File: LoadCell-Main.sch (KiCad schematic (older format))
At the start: 13 parts, among them J1 0.100_1X4, J2 22-27-2031, U1 LMV358

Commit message: Generated revA output files
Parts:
- gave numbers to parts that had none: 1
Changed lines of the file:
@@
 	5650 3650 5700 3650
 Wire Wire Line
-	5700 3950 5700 4000
-Wire Wire Line
-	5700 4000 5700 4050
+	5700 3950 5700 4050
 Wire Wire Line
 	5050 3750 5000 3750
@@
 Connection ~ 6250 4450
 Wire Wire Line
-	6900 3950 6900 4000
-Wire Wire Line
-	6900 4000 6900 4050
+	6900 3950 6900 4050
 Wire Wire Line
 	6900 4450 6900 4350
@@
 $EndComp
 Wire Wire Line
-	6650 3650 6700 3650
-Wire Wire Line
-	6700 3650 6900 3650
-Wire Wire Line
-	6900 3650 7150 3650
-Wire Wire Line
-	7150 3650 7450 3650
+	6650 3650 7450 3650
 Wire Wire Line
 	7750 4450 7750 4200
@@
 Connection ~ 7750 3250
 Wire Wire Line
-	8000 3350 8000 4450
-Wire Wire Line
-	8000 4450 8000 4600
+	8000 3350 8000 4600
 Wire Wire Line
 	8000 3350 8100 3350
@@
 	4700 3350 4700 4450
 Wire Wire Line
-	4700 4450 5250 4450
-Wire Wire Line
-	5250 4450 6250 4450
-Wire Wire Line
-	6250 4450 6900 4450
-Wire Wire Line
-	6900 4450 7150 4450
-Wire Wire Line
-	7150 4450 7450 4450
-Wire Wire Line
-	7450 4450 7750 4450
-Wire Wire Line
-	7750 4450 8000 4450
+	4700 4450 8000 4450
 Connection ~ 8000 4450
 Wire Wire Line
-	4300 3250 5250 3250
-Wire Wire Line
-	5250 3250 6250 3250
-Wire Wire Line
-	6250 3250 7750 3250
-Wire Wire Line
-	7750 3250 8100 3250
+	4300 3250 8100 3250
 $Comp
-L D_ZENER D?
+L D_ZENER D1
 U 1 1 5AEC7150
 P 7450 4050
-F 0 "D?" V 7350 4150 50  0000 C CNN
+F 0 "D1" V 7350 4150 50  0000 C CNN
 F 1 "MM3Z3V0ST1G" H 7600 4150 40  0000 C CNN
 F 2 "Diodes_SMD:D_SOD-323" V 8000 4000 50  0001 C CNN
@@
 $EndComp
 Wire Wire Line
-	7450 3950 7450 3650
-Wire Wire Line
-	7450 3650 7450 3450
+	7450 3450 7450 3950
 Wire Wire Line
 	7450 4150 7450 4450

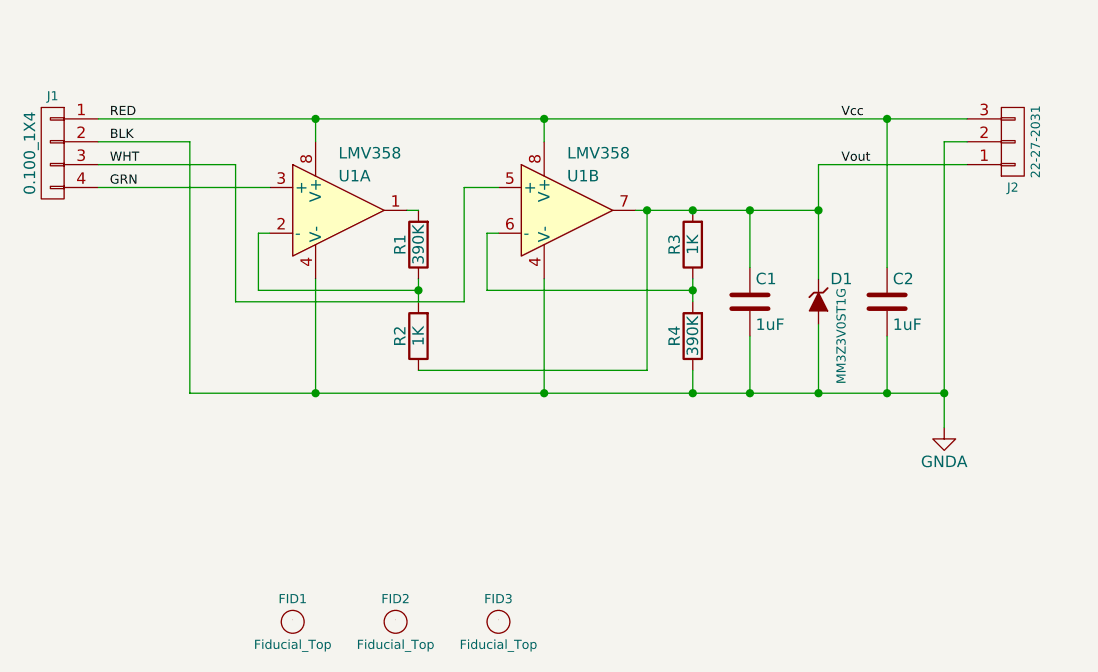
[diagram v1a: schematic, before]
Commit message: Corrected miswiring
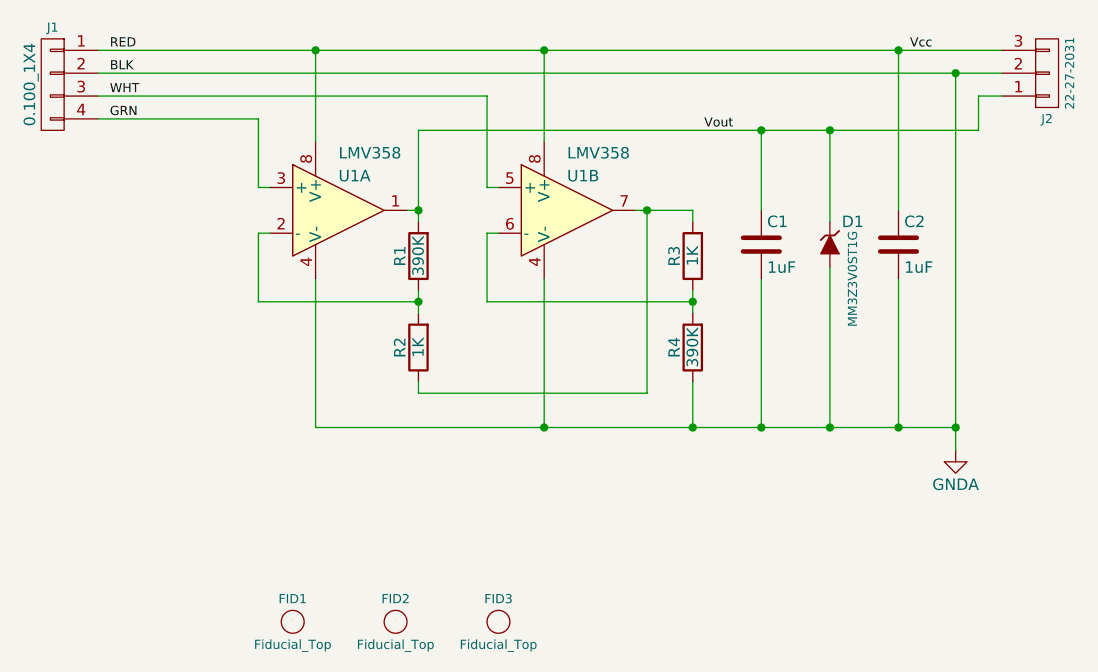
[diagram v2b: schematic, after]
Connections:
- net Vout: now also R1.2, U1.1; no longer R2.1, R3.2, U1.7
- new net: R2.1, R3.2, U1.7
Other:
- moved on the sheet: C1, C2, D1, J1, J2, R1, R2, R3, R4
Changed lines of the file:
@@
 L C C2
 U 1 1 5ADD8486
-P 7750 4050
-F 0 "C2" H 7775 4150 50  0000 L CNN
-F 1 "1uF" H 7775 3950 50  0000 L CNN
-F 2 "_Passive:C_0402" H 7788 3900 50  0001 C CNN
-F 3 "" H 7750 4050 50  0000 C CNN
-	1    7750 4050
+P 7800 3800
+F 0 "C2" H 7825 3900 50  0000 L CNN
+F 1 "1uF" H 7825 3700 50  0000 L CNN
+F 2 "_Passive:C_0402" H 7838 3650 50  0001 C CNN
+F 3 "" H 7800 3800 50  0000 C CNN
+	1    7800 3800
 	1    0    0    -1
 $EndComp
@@
 L C C1
 U 1 1 5ADD848C
-P 7150 4050
-F 0 "C1" H 7175 4150 50  0000 L CNN
-F 1 "1uF" H 7175 3950 50  0000 L CNN
-F 2 "_Passive:C_0402" H 7188 3900 50  0001 C CNN
-F 3 "" H 7150 4050 50  0000 C CNN
-	1    7150 4050
+P 7200 3800
+F 0 "C1" H 7225 3900 50  0000 L CNN
+F 1 "1uF" H 7225 3700 50  0000 L CNN
+F 2 "_Passive:C_0402" H 7238 3650 50  0001 C CNN
+F 3 "" H 7200 3800 50  0000 C CNN
+	1    7200 3800
 	1    0    0    -1
 $EndComp
@@
 L R R1
 U 1 1 5ADD8498
-P 5700 3800
-F 0 "R1" V 5780 3800 50  0000 C CNN
-F 1 "390K" V 5700 3800 50  0000 C CNN
-F 2 "_Passive:R_0402" V 5630 3800 50  0001 C CNN
-F 3 "" H 5700 3800 50  0000 C CNN
-	1    5700 3800
+P 5700 3850
+F 0 "R1" V 5780 3850 50  0000 C CNN
+F 1 "390K" V 5700 3850 50  0000 C CNN
+F 2 "_Passive:R_0402" V 5630 3850 50  0001 C CNN
+F 3 "" H 5700 3850 50  0000 C CNN
+	1    5700 3850
 	-1   0    0    1
 $EndComp
@@
 L R R2
 U 1 1 5ADD849E
-P 5700 4200
-F 0 "R2" V 5780 4200 50  0000 C CNN
-F 1 "1K" V 5700 4200 50  0000 C CNN
-F 2 "_Passive:R_0402" V 5630 4200 50  0001 C CNN
-F 3 "" H 5700 4200 50  0000 C CNN
-	1    5700 4200
-	-1   0    0    1
-$EndComp
-Text Label 7550 3250 0    40   ~ 0
+P 5700 4250
+F 0 "R2" V 5780 4250 50  0000 C CNN
+F 1 "1K" V 5700 4250 50  0000 C CNN
+F 2 "_Passive:R_0402" V 5630 4250 50  0001 C CNN
+F 3 "" H 5700 4250 50  0000 C CNN
+	1    5700 4250
+	-1   0    0    1
+$EndComp
+Text Label 7850 2950 0    40   ~ 0
 Vcc
-Text Label 7550 3450 0    40   ~ 0
+Text Label 6950 3300 0    40   ~ 0
 Vout
 $Comp
 L 0.100_1X4 J1
 U 1 1 5ADD84B2
-P 4100 3400
-F 0 "J1" H 4100 3650 40  0000 C CNN
-F 1 "0.100_1X4" V 4200 3400 50  0000 C CNN
-F 2 "Socket_Strips:Socket_Strip_Straight_1x04_Pitch2.00mm" H 4100 3400 50  0001 C CNN
-F 3 "" H 4100 3400 50  0000 C CNN
-	1    4100 3400
+P 4100 3100
+F 0 "J1" H 4100 3350 40  0000 C CNN
+F 1 "0.100_1X4" V 4200 3100 50  0000 C CNN
+F 2 "Socket_Strips:Socket_Strip_Straight_1x04_Pitch2.00mm" H 4100 3100 50  0001 C CNN
+F 3 "" H 4100 3100 50  0000 C CNN
+	1    4100 3100
 	-1   0    0    -1
 $EndComp
+Text Label 4350 2950 0    40   ~ 0
+RED
+Text Label 4350 3050 0    40   ~ 0
+BLK
 Text Label 4350 3250 0    40   ~ 0
-RED
-Text Label 4350 3350 0    40   ~ 0
-BLK
-Text Label 4350 3550 0    40   ~ 0
 GRN
-Text Label 4350 3450 0    40   ~ 0
+Text Label 4350 3150 0    40   ~ 0
 WHT
-Connection ~ 7150 4450
-Wire Wire Line
-	7150 4450 7150 4200
+Connection ~ 7200 4600
+Wire Wire Line
+	7200 4600 7200 3950
 $Comp
 L MCP6002 U1
@@
 $EndComp
 Wire Wire Line
-	5250 4450 5250 3950
-Connection ~ 5250 4450
-Wire Wire Line
-	5650 3650 5700 3650
-Wire Wire Line
-	5700 3950 5700 4050
+	5250 4600 5250 3950
+Wire Wire Line
+	5700 4000 5700 4100
 Wire Wire Line
 	5050 3750 5000 3750
 Wire Wire Line
-	5000 3750 5000 4000
-Wire Wire Line
-	5000 4000 5700 4000
-Connection ~ 5700 4000
-Wire Wire Line
-	4300 3550 5050 3550
+	5000 3750 5000 4050
+Wire Wire Line
+	5000 4050 5700 4050
+Connection ~ 5700 4050
 $Comp
 L R R3
 U 1 1 5ADD84E0
-P 6900 3800
-F 0 "R3" V 6980 3800 50  0000 C CNN
-F 1 "1K" V 6900 3800 50  0000 C CNN
-F 2 "_Passive:R_0402" V 6830 3800 50  0001 C CNN
-F 3 "" H 6900 3800 50  0000 C CNN
-	1    6900 3800
+P 6900 3850
+F 0 "R3" V 6980 3850 50  0000 C CNN
+F 1 "1K" V 6900 3850 50  0000 C CNN
+F 2 "_Passive:R_0402" V 6830 3850 50  0001 C CNN
+F 3 "" H 6900 3850 50  0000 C CNN
+	1    6900 3850
 	-1   0    0    1
 $EndComp
@@
 L R R4
 U 1 1 5ADD84E6
-P 6900 4200
-F 0 "R4" V 6980 4200 50  0000 C CNN
-F 1 "390K" V 6900 4200 50  0000 C CNN
-F 2 "_Passive:R_0402" V 6830 4200 50  0001 C CNN
-F 3 "" H 6900 4200 50  0000 C CNN
-	1    6900 4200
-	-1   0    0    1
-$EndComp
-Wire Wire Line
-	5250 3350 5250 3250
-Connection ~ 5250 3250
-Wire Wire Line
-	6250 3250 6250 3350
-Connection ~ 6250 3250
-Wire Wire Line
-	6250 4450 6250 3950
-Connection ~ 6250 4450
-Wire Wire Line
-	6900 3950 6900 4050
-Wire Wire Line
-	6900 4450 6900 4350
-Connection ~ 6900 4450
-Wire Wire Line
-	5700 4350 6700 4350
-Wire Wire Line
-	6700 4350 6700 3650
+P 6900 4250
+F 0 "R4" V 6980 4250 50  0000 C CNN
+F 1 "390K" V 6900 4250 50  0000 C CNN
+F 2 "_Passive:R_0402" V 6830 4250 50  0001 C CNN
+F 3 "" H 6900 4250 50  0000 C CNN
+	1    6900 4250
+	-1   0    0    1
+$EndComp
+Wire Wire Line
+	5250 3350 5250 2950
+Connection ~ 5250 2950
+Wire Wire Line
+	6250 2950 6250 3350
+Connection ~ 6250 2950
+Wire Wire Line
+	6250 4600 6250 3950
+Connection ~ 6250 4600
+Wire Wire Line
+	6900 4000 6900 4100
+Wire Wire Line
+	6900 4600 6900 4400
+Connection ~ 6900 4600
+Wire Wire Line
+	6700 4450 6700 3650
 Connection ~ 6700 3650
 Wire Wire Line
-	4900 4050 5900 4050
-Wire Wire Line
-	5900 4050 5900 3550
-Wire Wire Line
-	5900 3550 6050 3550
+	6000 3550 6050 3550
 Wire Wire Line
 	6050 3750 6000 3750
 Wire Wire Line
-	6000 3750 6000 4000
-Wire Wire Line
-	6000 4000 6900 4000
-Connection ~ 6900 4000
-Connection ~ 6900 3650
-Connection ~ 7150 3650
+	6000 3750 6000 4050
+Wire Wire Line
+	6000 4050 6900 4050
+Connection ~ 6900 4050
 $Comp
 L 22-27-2031 J2
 U 1 1 5AEC5795
-P 8300 3350
-F 0 "J2" H 8300 3550 40  0000 C CNN
-F 1 "22-27-2031" V 8400 3350 40  0000 C CNN
-F 2 "_Connector:0.100_1x3_small" H 8300 3350 50  0001 C CNN
-F 3 "" H 8300 3350 50  0000 C CNN
-	1    8300 3350
+P 8450 3050
+F 0 "J2" H 8450 3250 40  0000 C CNN
+F 1 "22-27-2031" V 8550 3050 40  0000 C CNN
+F 2 "_Connector:0.100_1x3_small" H 8450 3050 50  0001 C CNN
+F 3 "" H 8450 3050 50  0000 C CNN
+	1    8450 3050
 	1    0    0    1
 $EndComp
@@
 L GNDA #PWR01
 U 1 1 5AEC5B25
-P 8000 4600
-F 0 "#PWR01" H 8000 4350 50  0001 C CNN
-F 1 "GNDA" H 8000 4450 50  0000 C CNN
-F 2 "" H 8000 4600 50  0000 C CNN
-F 3 "" H 8000 4600 50  0000 C CNN
-	1    8000 4600
-	1    0    0    -1
-$EndComp
-Wire Wire Line
-	6650 3650 7450 3650
-Wire Wire Line
-	7750 4450 7750 4200
-Wire Wire Line
-	7750 3250 7750 3900
-Connection ~ 7750 3250
-Wire Wire Line
-	8000 3350 8000 4600
-Wire Wire Line
-	8000 3350 8100 3350
-Connection ~ 7750 4450
-Wire Wire Line
-	4300 3450 4900 3450
-Wire Wire Line
-	4900 3450 4900 4050
-Wire Wire Line
-	4300 3350 4700 3350
-Wire Wire Line
-	4700 3350 4700 4450
-Wire Wire Line
-	4700 4450 8000 4450
-Connection ~ 8000 4450
-Wire Wire Line
-	4300 3250 8100 3250
+P 8050 4700
+F 0 "#PWR01" H 8050 4450 50  0001 C CNN
+F 1 "GNDA" H 8050 4550 50  0000 C CNN
+F 2 "" H 8050 4700 50  0000 C CNN
+F 3 "" H 8050 4700 50  0000 C CNN
+	1    8050 4700
+	1    0    0    -1
+$EndComp
+Wire Wire Line
+	6650 3650 6900 3650
+Wire Wire Line
+	7800 4600 7800 3950
+Wire Wire Line
+	7800 2950 7800 3650
+Connection ~ 7800 2950
+Wire Wire Line
+	8050 3050 8050 4700
+Connection ~ 7800 4600
+Wire Wire Line
+	4300 3150 6000 3150
+Wire Wire Line
+	4300 3050 8250 3050
+Connection ~ 8050 4600
+Wire Wire Line
+	4300 2950 8250 2950
 $Comp
 L D_ZENER D1
 U 1 1 5AEC7150
-P 7450 4050
-F 0 "D1" V 7350 4150 50  0000 C CNN
-F 1 "MM3Z3V0ST1G" H 7600 4150 40  0000 C CNN
-F 2 "Diodes_SMD:D_SOD-323" V 8000 4000 50  0001 C CNN
-F 3 "" H 7450 4050 50  0000 C CNN
-	1    7450 4050
+P 7500 3800
+F 0 "D1" V 7400 3900 50  0000 C CNN
+F 1 "MM3Z3V0ST1G" H 7650 3900 40  0000 C CNN
+F 2 "Diodes_SMD:D_SOD-323" V 8050 3750 50  0001 C CNN
+F 3 "" H 7500 3800 50  0000 C CNN
+	1    7500 3800
 	0    1    1    0
 $EndComp
 Wire Wire Line
-	7450 3450 7450 3950
-Wire Wire Line
-	7450 4150 7450 4450
-Connection ~ 7450 4450
-Connection ~ 7450 3650
-Wire Wire Line
-	7450 3450 8100 3450
-Wire Wire Line
-	7150 3900 7150 3650
+	7500 4600 7500 3900
+Connection ~ 7500 4600
+Wire Wire Line
+	7200 3300 7200 3650
+Wire Wire Line
+	4300 3250 5000 3250
+Wire Wire Line
+	5000 3250 5000 3550
+Wire Wire Line
+	5000 3550 5050 3550
+Wire Wire Line
+	5700 3300 5700 3700
+Wire Wire Line
+	5700 3300 8150 3300
+Connection ~ 7200 3300
+Wire Wire Line
+	7500 3300 7500 3700
+Connection ~ 7500 3300
+Wire Wire Line
+	5650 3650 5700 3650
+Connection ~ 5700 3650
+Wire Wire Line
+	6900 3650 6900 3700
+Wire Wire Line
+	8150 3300 8150 3150
+Wire Wire Line
+	8150 3150 8250 3150
+Wire Wire Line
+	6000 3150 6000 3550
+Wire Wire Line
+	5700 4400 5700 4450
+Wire Wire Line
+	5700 4450 6700 4450
+Connection ~ 8050 3050
+Wire Wire Line
+	5250 4600 8050 4600
 $EndSCHEMATC
